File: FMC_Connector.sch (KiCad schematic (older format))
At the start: 1 part, among them J1 ASP-134488-01

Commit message: before re-arranging
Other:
- note added: "NOTE!! I (i) and J rows in FMC HPC symbol correspond to footprint row J K because no I (i) row in footprint"
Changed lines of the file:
@@
 Wire Wire Line
 	1950 1350 1950 1450
+Text Notes 1400 -100 0    59   ~ 12
+NOTE!!  I (i) and J rows in FMC HPC symbol  correspond to footprint row J K because no I (i) row in footprint
 $EndSCHEMATC

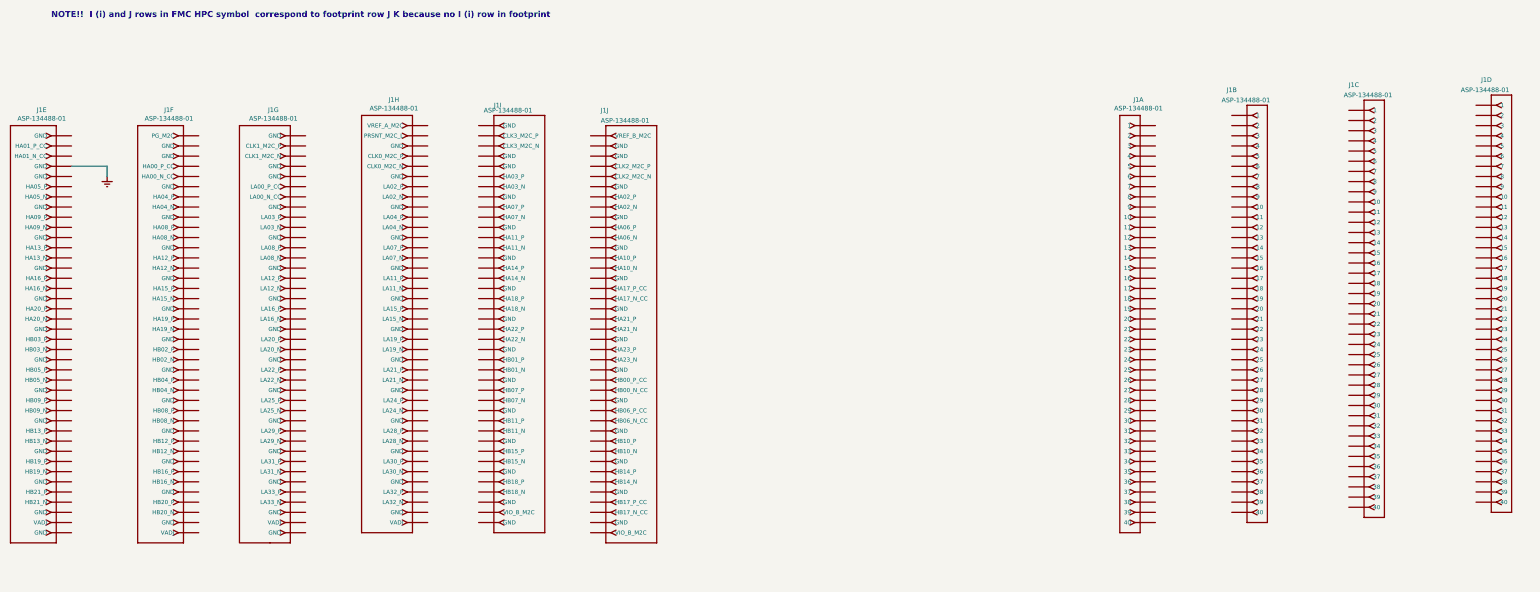
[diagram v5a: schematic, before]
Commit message: fixed 3.3 volt level shifter
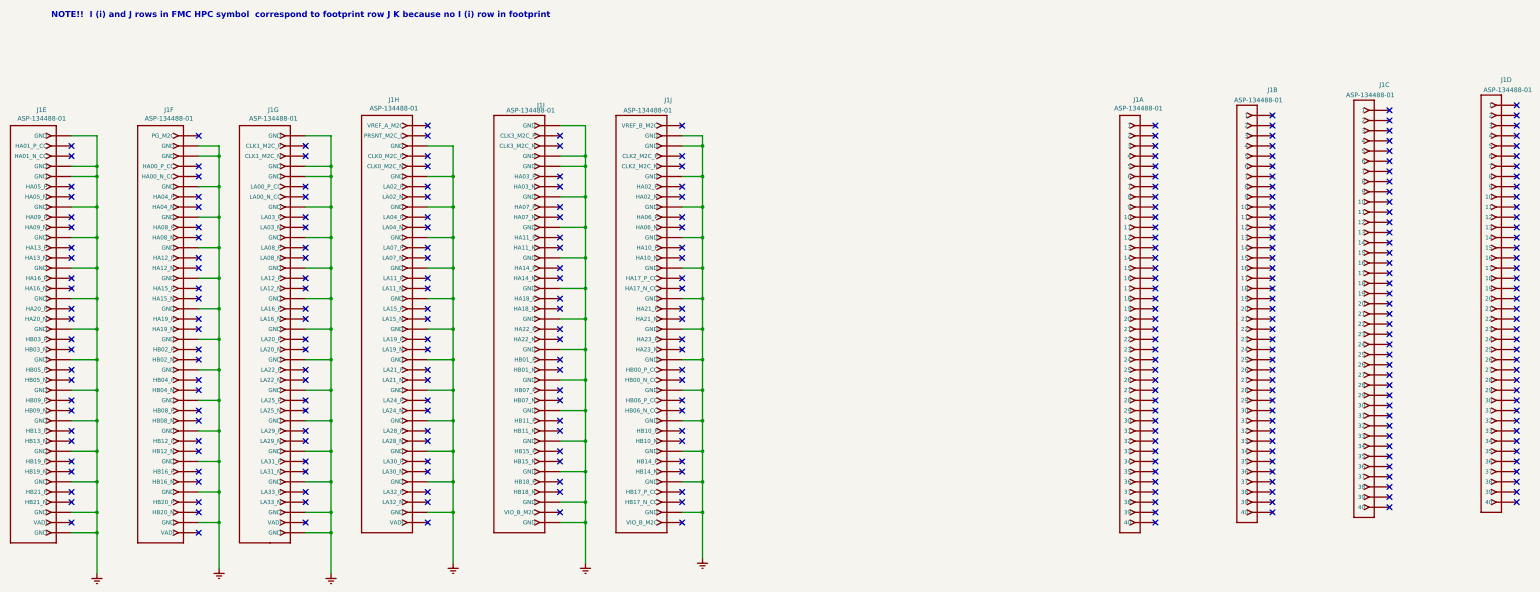
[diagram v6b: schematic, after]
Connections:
- net Earth: now also J1.E1 (GND), J1.E11 (GND), J1.E14 (GND), J1.E17 (GND), J1.E20 (GND), J1.E23 (GND), J1.E26 (GND), J1.E29 (GND), J1.E32 (GND), J1.E35 (GND), J1.E38 (GND), J1.E40 (GND), J1.E5 (GND), J1.E8 (GND), J1.F12 (GND), J1.F15 (GND), J1.F18 (GND), J1.F2 (GND), J1.F21 (GND), J1.F24 (GND), J1.F27 (GND), J1.F3 (GND), J1.F30 (GND), J1.F33 (GND), J1.F36 (GND), J1.F39 (GND), J1.F6 (GND), J1.F9 (GND), J1.G1 (GND), J1.G11 (GND), J1.G14 (GND), J1.G17 (GND), J1.G20 (GND), J1.G23 (GND), J1.G26 (GND), J1.G29 (GND), J1.G32 (GND), J1.G35 (GND), J1.G38 (GND), J1.G4 (GND), J1.G40 (GND), J1.G5 (GND), J1.G8 (GND), J1.H12 (GND), J1.H15 (GND), J1.H18 (GND), J1.H21 (GND), J1.H24 (GND), J1.H27 (GND), J1.H3 (GND), J1.H30 (GND), J1.H33 (GND), J1.H36 (GND), J1.H39 (GND), J1.H6 (GND), J1.H9 (GND), J1.J1 (GND), J1.J11 (GND), J1.J14 (GND), J1.J17 (GND), J1.J20 (GND), J1.J23 (GND), J1.J26 (GND), J1.J29 (GND), J1.J32 (GND), J1.J35 (GND), J1.J38 (GND), J1.J4 (GND), J1.J40 (GND), J1.J5 (GND), J1.J8 (GND), J1.K12 (GND), J1.K15 (GND), J1.K18 (GND), J1.K2 (GND), J1.K21 (GND), J1.K24 (GND), J1.K27 (GND), J1.K3 (GND), J1.K30 (GND), J1.K33 (GND), J1.K36 (GND), J1.K39 (GND), J1.K6 (GND), J1.K9 (GND)
- no-connect marks 0 -> 314
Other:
- moved on the sheet: J1B, J1C, J1D, J1I, J1J
